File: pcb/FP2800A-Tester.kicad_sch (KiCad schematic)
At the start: 4 parts, among them SW1 Reset, U1 FP2800A

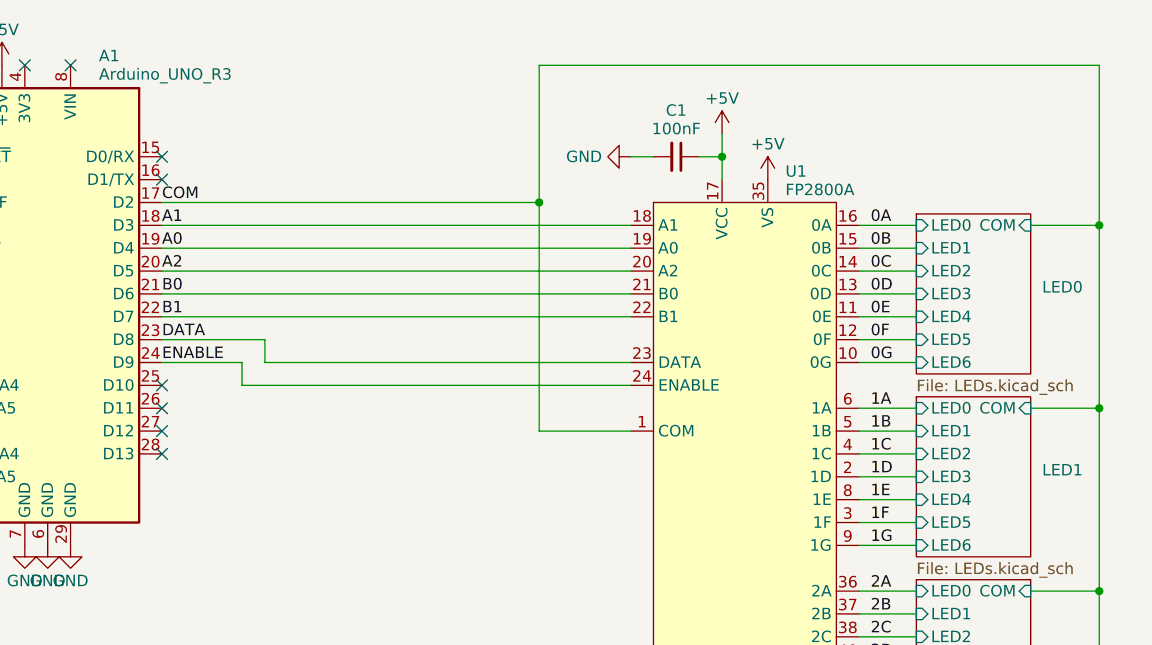
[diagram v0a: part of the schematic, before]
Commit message: feat: add COM Jumper
Add a jumper that allows to disconnect the FP2800A COM pin from the LEDs
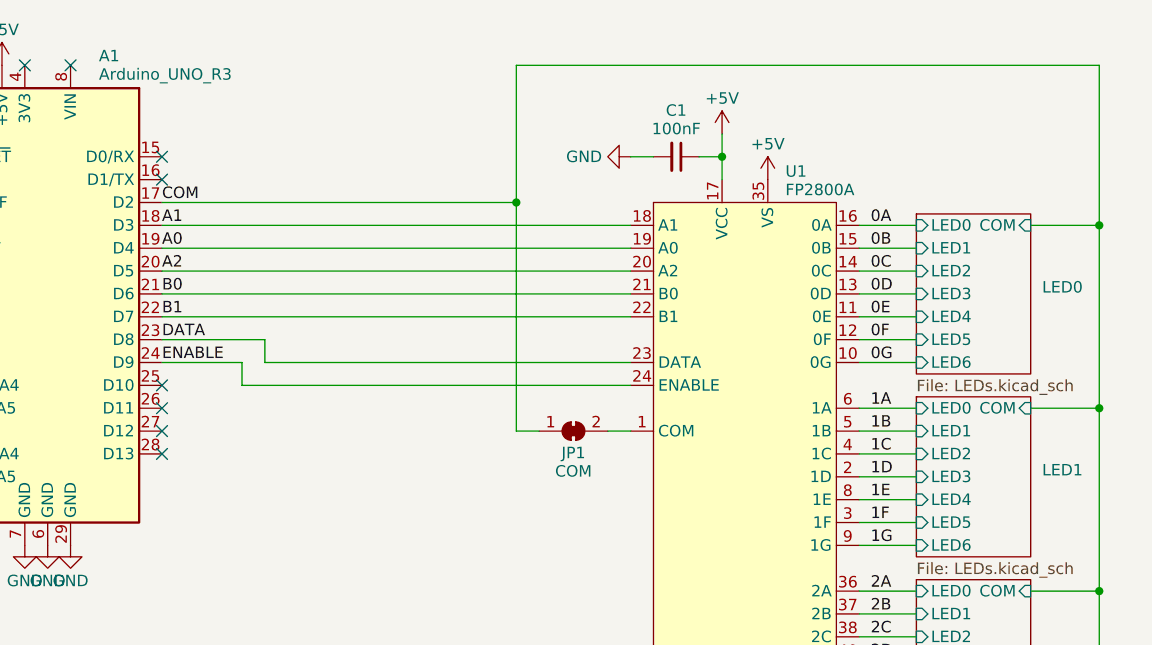
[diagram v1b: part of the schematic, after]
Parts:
- added JP1: COM, Jumper:SolderJumper-2_P1.3mm_Bridged_RoundedPad1.0x1.5mm, symbol Jumper:SolderJumper_2_Bridged
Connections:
- net COM: now also JP1.1 (A); no longer U1.1 (COM)
- new net: JP1.2 (B), U1.1 (COM)
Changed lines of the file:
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@@
   (junction (at 210.82 97.79) (diameter 0) (color 0 0 0 0)
   )
-  (junction (at 148.59 54.61) (diameter 0) (color 0 0 0 0)
+  (junction (at 146.05 54.61) (diameter 0) (color 0 0 0 0)
   )
   (junction (at 210.82 57.15) (diameter 0) (color 0 0 0 0)
@@
     (stroke (width 0) (type default))
   )
-  (wire (pts (xy 106.68 54.61) (xy 148.59 54.61))
+  (wire (pts (xy 106.68 54.61) (xy 146.05 54.61))
     (stroke (width 0) (type default))
   )
@@
     (stroke (width 0) (type default))
   )
-  (wire (pts (xy 210.82 39.37) (xy 148.59 39.37))
+  (wire (pts (xy 210.82 39.37) (xy 146.05 39.37))
     (stroke (width 0) (type default))
   )
@@
     (stroke (width 0) (type default))
   )
+  (wire (pts (xy 156.21 80.01) (xy 158.75 80.01))
+    (stroke (width 0) (type default))
+  )
   (wire (pts (xy 184.15 113.03) (xy 190.5 113.03))
     (stroke (width 0) (type default))
   )
-  (wire (pts (xy 148.59 80.01) (xy 148.59 54.61))
-    (stroke (width 0) (type default))
-  )
-  (wire (pts (xy 158.75 80.01) (xy 148.59 80.01))
+  (wire (pts (xy 146.05 80.01) (xy 146.05 54.61))
     (stroke (width 0) (type default))
   )
@@
     (stroke (width 0) (type default))
   )
+  (wire (pts (xy 146.05 80.01) (xy 148.59 80.01))
+    (stroke (width 0) (type default))
+  )
   (wire (pts (xy 210.82 57.15) (xy 210.82 39.37))
     (stroke (width 0) (type default))
@@
     (stroke (width 0) (type default))
   )
-  (wire (pts (xy 148.59 39.37) (xy 148.59 54.61))
+  (wire (pts (xy 146.05 39.37) (xy 146.05 54.61))
     (stroke (width 0) (type default))
   )
@@
         )
       )
+    )
+  )
+  (symbol (lib_id "Jumper:SolderJumper_2_Bridged") (at 152.4 80.01 0) (unit 1)
+    (in_bom yes) (on_board yes) (dnp no) (fields_autoplaced)
+    (property "Reference" "JP1" (at 152.4 82.431 0)
+      (effects (font (size 1.27 1.27)))
+    )
+    (property "Value" "COM" (at 152.4 84.479 0)
+      (effects (font (size 1.27 1.27)))
+    )
+    (property "Footprint" "Jumper:SolderJumper-2_P1.3mm_Bridged_RoundedPad1.0x1.5mm" (at 152.4 80.01 0)
+      (effects (font (size 1.27 1.27)) hide)
+    )
+    (property "Datasheet" "~" (at 152.4 80.01 0)
+      (effects (font (size 1.27 1.27)) hide)
+    )
+    (pin "1")
+    (pin "2")
+    (instances
+      (project "FP2800A-Tester"
+        (path "/f519d2ac-5f22-4d49-955c-96b00ec489ca"
+          (reference "JP1") (unit 1)
+        )
+      )

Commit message: feat: replace IC socket with ZIF socket
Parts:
- U1: footprint Package_DIP:DIP-40_W15.24mm_Socket -> Socket:DIP_Socket-40_W11.9_W12.7_W15.24_W17.78_W18.5_3M_240-1280-00-0602J
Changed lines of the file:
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@@
       (effects (font (size 1.27 1.27)) (justify left))
     )
-    (property "Footprint" "Package_DIP:DIP-40_W15.24mm_Socket" (at 171.45 49.53 0)
+    (property "Footprint" "Socket:DIP_Socket-40_W11.9_W12.7_W15.24_W17.78_W18.5_3M_240-1280-00-0602J" (at 171.45 49.53 0)
       (effects (font (size 1.27 1.27)) hide)
     )
